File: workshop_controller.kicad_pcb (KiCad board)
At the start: 4 copper layers, 184.9 x 88 mm, 56 parts, among them J1 Conn_02x10_Odd_Even, J2 Conn_02x10_Odd_Even, J3 AudioJack4, J4 Micro_SD_Card, J5 Conn_02x25_Odd_Even, J6 Conn_01x05_Female, J7 LOGO_TOUCH, M1 Microphone4, SW1 SW_Push, SW2 SW_Push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

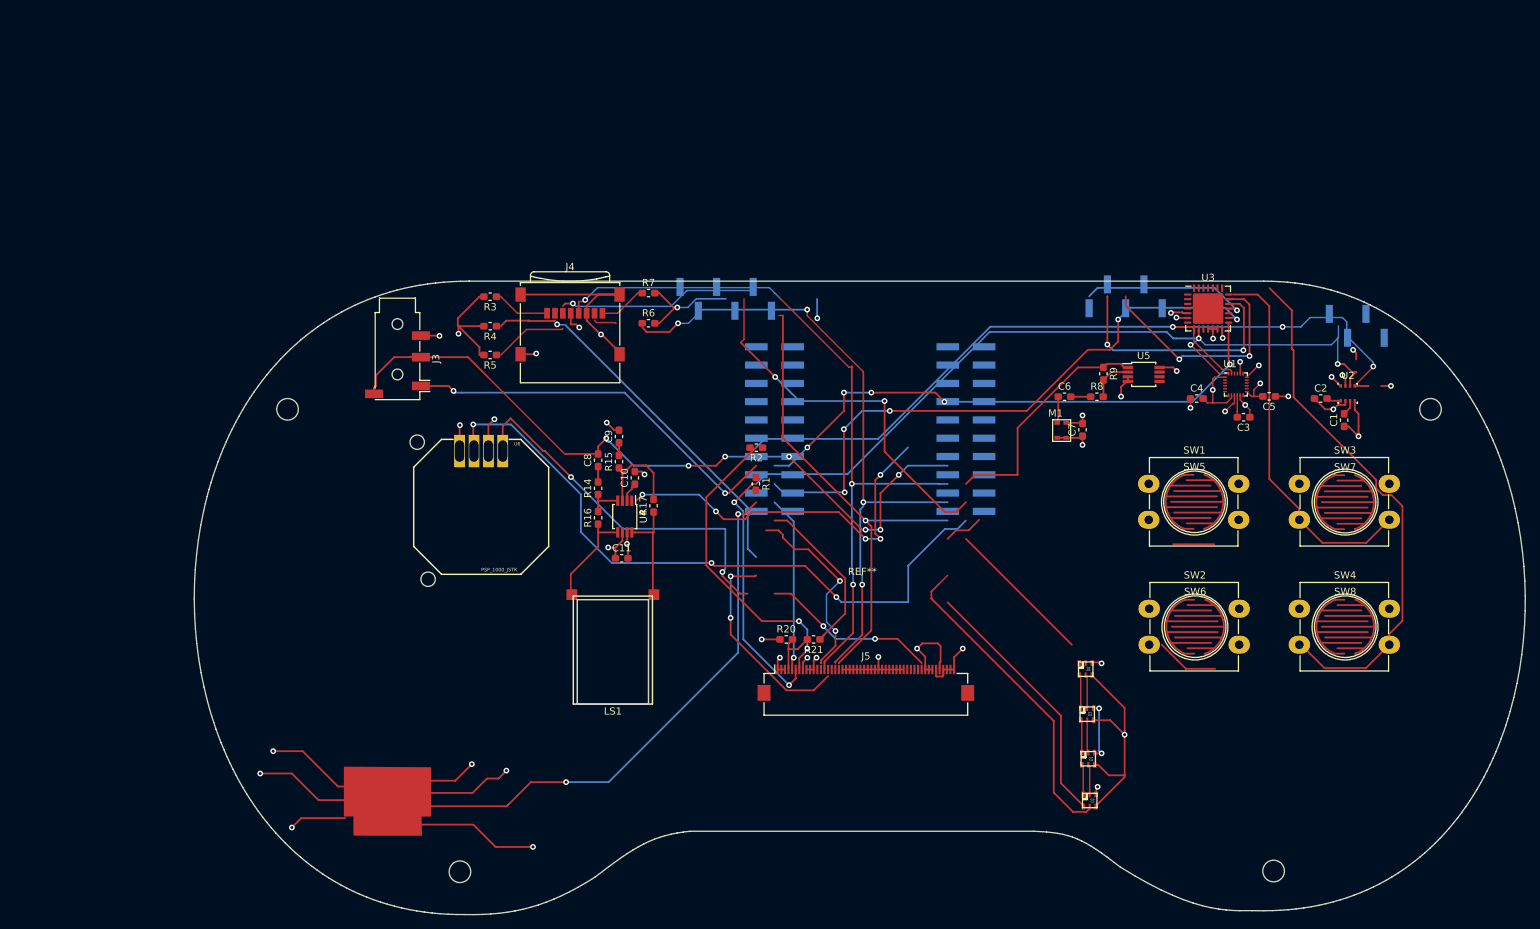
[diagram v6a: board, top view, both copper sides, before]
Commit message: Delete tracks
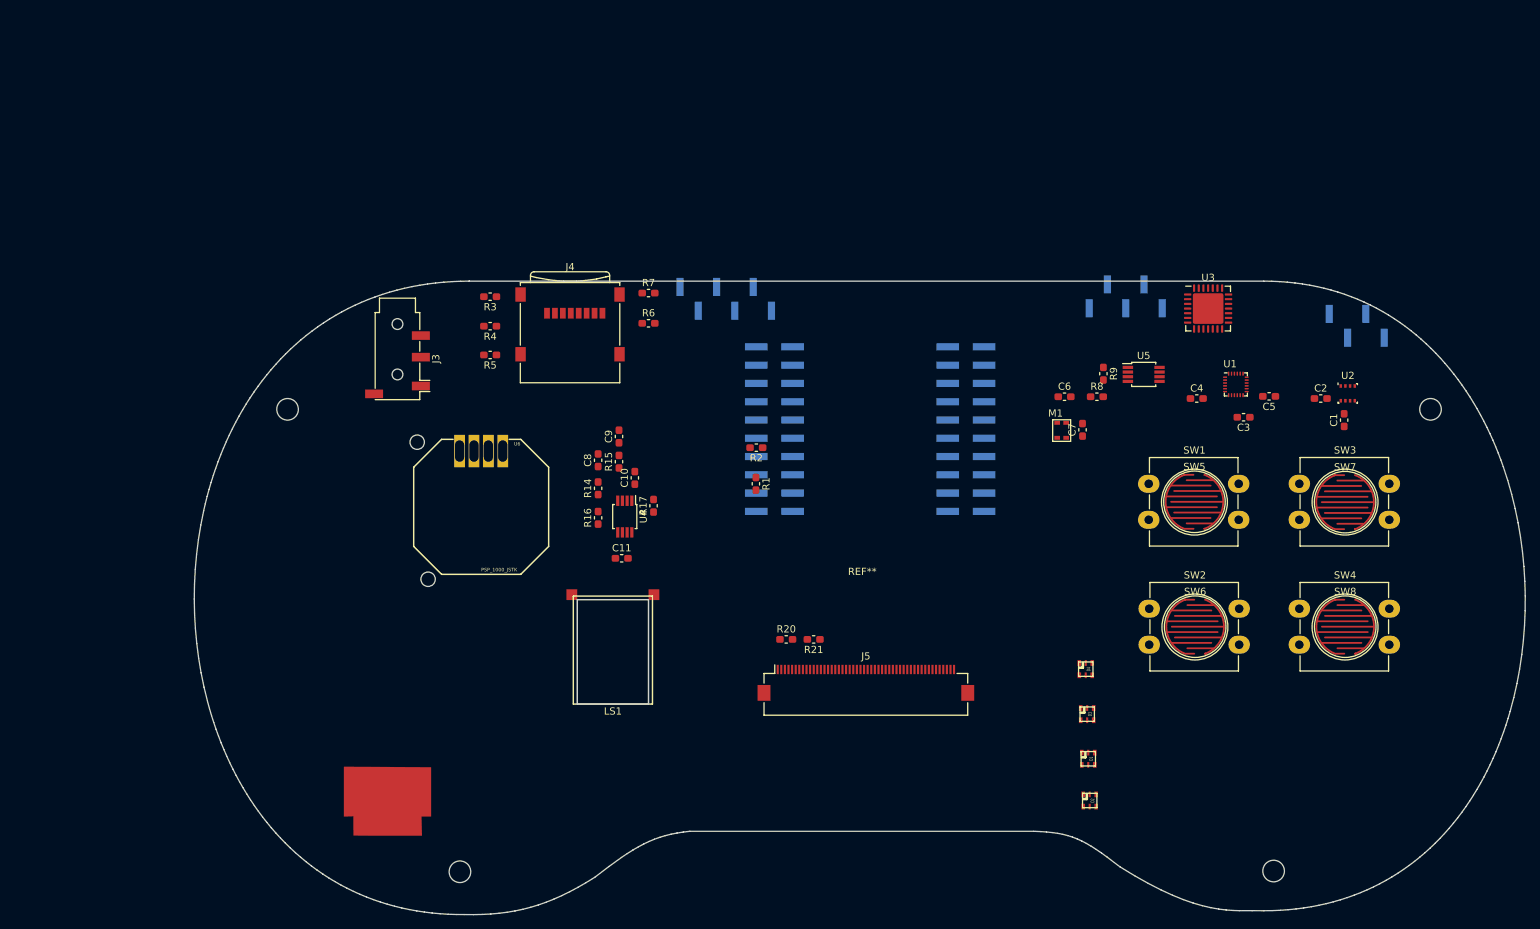
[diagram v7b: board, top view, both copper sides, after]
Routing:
- net /I2C_SCK: track 158.3 -> 0.00 mm, vias 5 -> 0
- net /I2C_SDA: track 146.3 -> 0.00 mm, vias 5 -> 0
- net GND: track 141.6 -> 0.00 mm, vias 26 -> 0
- net /GE_INTA: track 136.5 -> 0.00 mm, vias 7 -> 0
- net /PIN_23: track 105.1 -> 0.00 mm, vias 2 -> 0
- net /PIN_26: track 103.2 -> 0.00 mm, vias 7 -> 0
- net /PIN_18: track 102.1 -> 0.00 mm, vias 3 -> 0
- net +3V3: track 100.7 -> 0.00 mm, vias 21 -> 0
- net /PIN_19: track 93.8 -> 0.00 mm, vias 4 -> 0
- net /JOY_Y: track 93.1 -> 0.00 mm, vias 3 -> 0
- net /GE_INTB: track 77.5 -> 0.00 mm, vias 5 -> 0
- net /PIN_LOGO_TOUCH: track 74.8 -> 0.00 mm, vias 2 -> 0
- net /SW4_PIN: track 73.8 -> 0.00 mm
- net (no net): track 69.8 -> 0.00 mm, vias 6 -> 0
- net /PIN_25: track 54.3 -> 0.00 mm, vias 2 -> 0
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
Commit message: Redesign layout
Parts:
- added SW10: SW_Push, Hackheim_logo:contact_snes_button, F.Cu at (87.8, 81.6)
- added SW11: SW_Push, Hackheim_logo:contact_snes_button, F.Cu at (105.8, 81.7)
- added SW12: SW_Push, Hackheim_logo:contact_snes_button, F.Cu at (96.8, 90.7)
- added SW9: SW_Push, Hackheim_logo:contact_snes_button, F.Cu at (96.7, 72.7)
- moved LS1 108.9 mm to (219.7, 67.3), turned to 270 degrees
- moved U2 108.7 mm to (123.2, 113.1)
- moved C1 108.7 mm to (122.7, 116.8)
- moved C2 108.7 mm to (119.5, 113.8)
- moved D1 100.6 mm to (140.8, 29.7)
- moved D2 100.6 mm to (141.0, 35.5)
- moved D4 100.6 mm to (140.4, 17.3)
- moved D3 100.6 mm to (140.6, 23.5)
- moved C3 90.8 mm to (121.5, 99.6)
- moved C5 90.8 mm to (125.0, 96.7)
- moved U1 90.8 mm to (120.4, 95.1)
- moved C4 89.1 mm to (116.1, 95.1)
- moved U3 84.2 mm to (121.2, 77.2)
- moved C11 83.9 mm to (201.0, 64.5), turned to 180 degrees
- moved R16 80.9 mm to (198.0, 72.7), turned to 180 degrees
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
